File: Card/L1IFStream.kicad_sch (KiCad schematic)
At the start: 109 parts, among them J1 Conn_Coaxial, J2 USB_A, J3 RF_Shield_One_Piece, J4 Conn_Coaxial, U1 MAX2769BETI+T, U10 74LVC374, U11 74HC2GU04, U2 TPS717285DCK, U3 TPS717285DCK, U4 NCP164CSN330T1G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

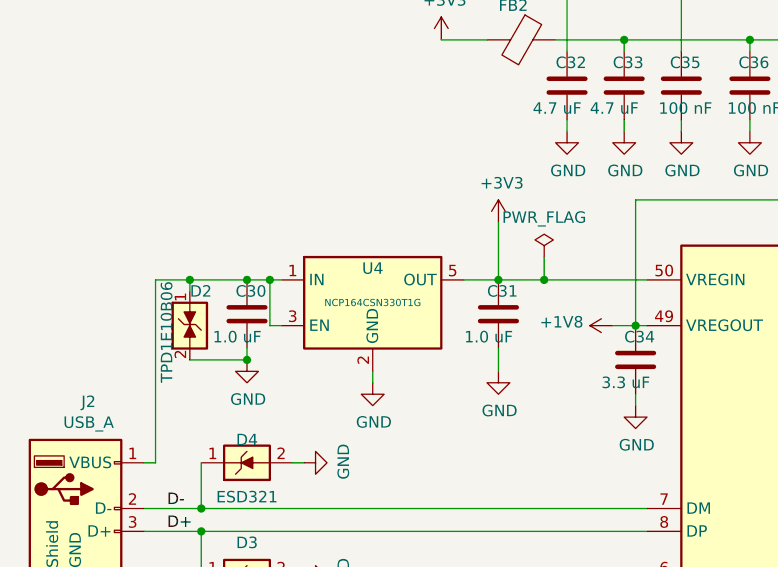
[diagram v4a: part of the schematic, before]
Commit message: Library clean up through U4
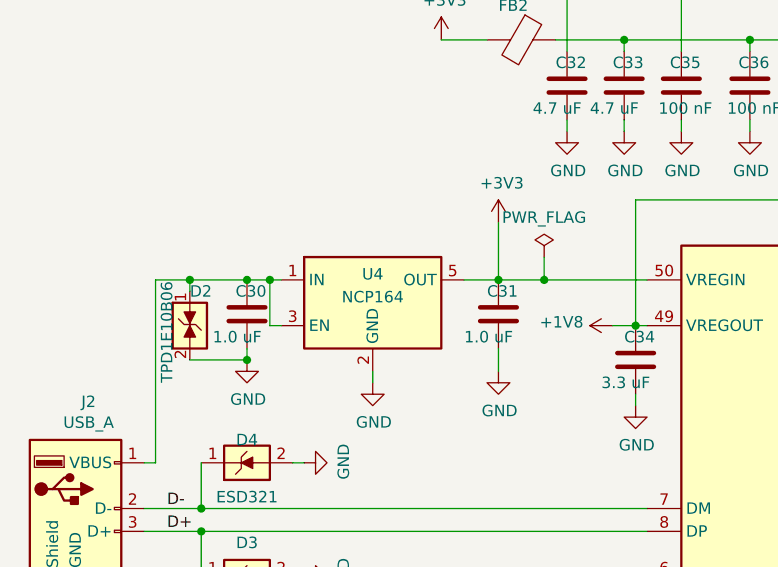
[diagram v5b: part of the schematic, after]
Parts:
- removed U4: NCP164CSN330T1G, L1IFStream:TSOT-23-5, symbol L1IFStream-rescue:NCP164CSN330T1G-MAX2769FT2232H
- added U4: NCP164, L1IF:TSOP-5, symbol L1IF:NCP164CSN330T1G
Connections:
- net +3V3: now also U4.5 (OUT)
- net GND: now also U4.2 (GND)
- net at C30.1, D2.1 (K), J2.1 (VBUS): now also U4.1 (IN), U4.3 (EN)
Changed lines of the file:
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@@
-    )
-  )
-  (symbol (lib_id "L1IFStream-rescue:NCP164CSN330T1G-MAX2769FT2232H") (at 53.34 64.77 0) (unit 1)
-    (in_bom yes) (on_board yes) (dnp no)
-    (property "Reference" "U4" (at 53.34 60.96 0)
-      (effects (font (size 1.27 1.27)))
-    )
-    (property "Value" "NCP164CSN330T1G" (at 53.34 64.77 0)
-      (effects (font (size 0.7874 0.7874)))
-    )
-    (property "Footprint" "L1IFStream:TSOT-23-5" (at 53.34 74.93 0)
-      (effects (font (size 1.27 1.27) italic) hide)
-    )
-    (property "Datasheet" "https://www.onsemi.com/pub/Collateral/NCP164C-D.PDF" (at 53.34 77.47 0)
-      (effects (font (size 1.27 1.27)) hide)
-    )
-    (property "Description" "LDO 300 MA AD 3.3V, ULTRA" (at 53.34 64.77 0)
-      (effects (font (size 1.27 1.27)) hide)
-    )
-    (property "Manufacturer" "Onsemi" (at 53.34 64.77 0)
-      (effects (font (size 1.27 1.27)) hide)
-    )
-    (property "MPN" "NCP164CSN330T1G" (at 53.34 64.77 0)
-      (effects (font (size 1.27 1.27)) hide)
-    )
-    (property "Vendor" "DigiKey" (at 53.34 64.77 0)
-      (effects (font (size 1.27 1.27)) hide)
-    )
-    (property "Vendor P/N#" "488-NCP164CSN330T1GCT-ND" (at 53.34 64.77 0)
-      (effects (font (size 1.27 1.27)) hide)
-    )
-    (property "Notes" "Alternate: AP2127K-ADJTRG1DIDKR-ND" (at 53.34 64.77 0)
-      (effects (font (size 1.27 1.27)) hide)
-    )
-    (property "Alternate" "https://www.diodes.com/assets/Datasheets/AP2127.pdf" (at 53.34 64.77 0)
-      (effects (font (size 1.27 1.27)) hide)
-    )
-    (pin "1")
-    (pin "2")
-    (pin "3")
-    (pin "4")
-    (pin "5")
-    (instances
-      (project "L1IFStream"
-        (path "/e22d8814-0b83-456b-8939-db783783fcf1"
-          (reference "U4") (unit 1)
-        )
-      )
     )
   )
@@
         )
       )
+    )
+  )
+  (symbol (lib_name "NCP164CSN330T1G_1") (lib_id "L1IF:NCP164CSN330T1G") (at 53.34 64.77 0) (unit 1)
+    (in_bom yes) (on_board yes) (dnp no)
+    (property "Reference" "U4" (at 53.34 61.595 0)
+      (effects (font (size 1.27 1.27)))
+    )
+    (property "Value" "NCP164" (at 53.34 64.135 0)
+      (effects (font (size 1.27 1.27)))
+    )
+    (property "Footprint" "L1IF:TSOP-5" (at 53.34 74.93 0)
+      (effects (font (size 1.27 1.27) italic) hide)
+    )
+    (property "Datasheet" "https://www.onsemi.com/pub/Collateral/NCP164C-D.PDF" (at 53.34 77.47 0)
+      (effects (font (size 1.27 1.27)) hide)
+    )
+    (property "Manufacturer" "Onsemi" (at 53.34 46.99 0)
+      (effects (font (size 1.27 1.27)) hide)
+    )
+    (property "MPN" "NCP164CSN330T1G" (at 53.34 49.53 0)
+      (effects (font (size 1.27 1.27)) hide)
+    )
+    (property "Vendor" "DigiKey" (at 53.34 52.07 0)
+      (effects (font (size 1.27 1.27)) hide)
+    )
+    (property "Vendor PN" "488-NCP164CSN330T1GCT-ND" (at 54.61 54.61 0)
+      (effects (font (size 1.27 1.27)) hide)
+    )
+    (pin "1")
+    (pin "2")
+    (pin "3")
+    (pin "4")
+    (pin "5")
+    (instances
+      (project "L1IFStream"
+        (path "/e22d8814-0b83-456b-8939-db783783fcf1"
+          (reference "U4") (unit 1)
+        )
+      )
